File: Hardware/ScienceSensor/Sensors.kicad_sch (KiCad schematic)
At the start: 41 parts, among them J1 USB_A, Q2 BSS138, Q4 BSS138, U4 FT230XS

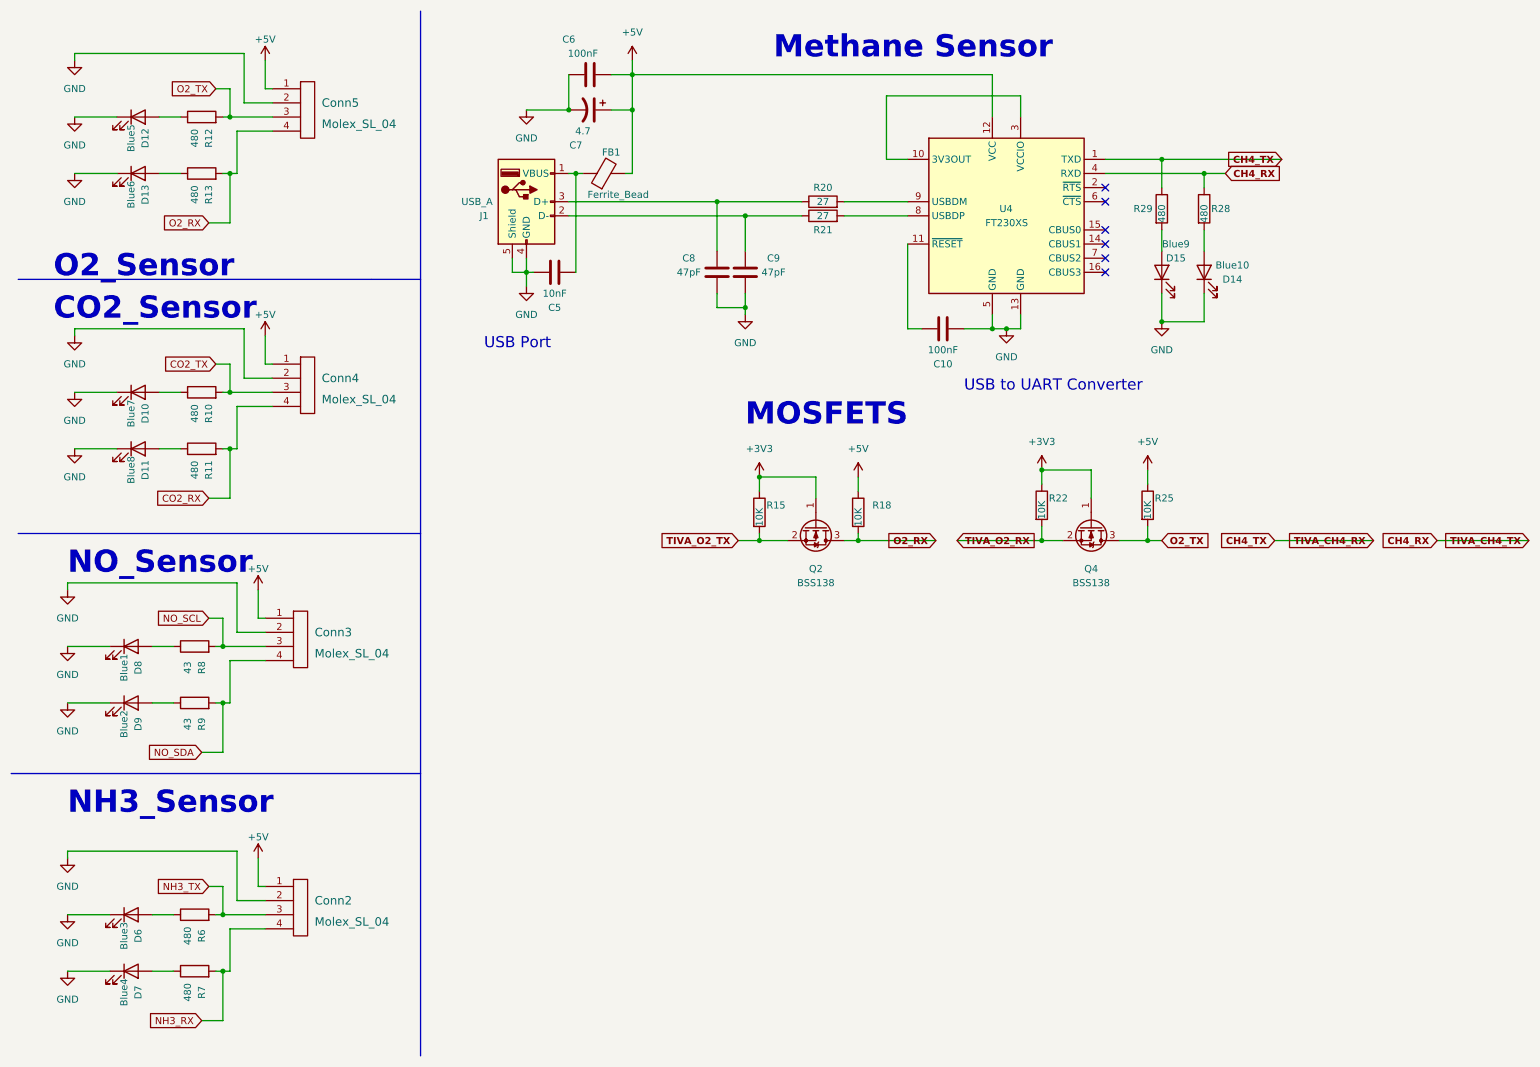
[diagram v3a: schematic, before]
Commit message: Fixed diode ref / values
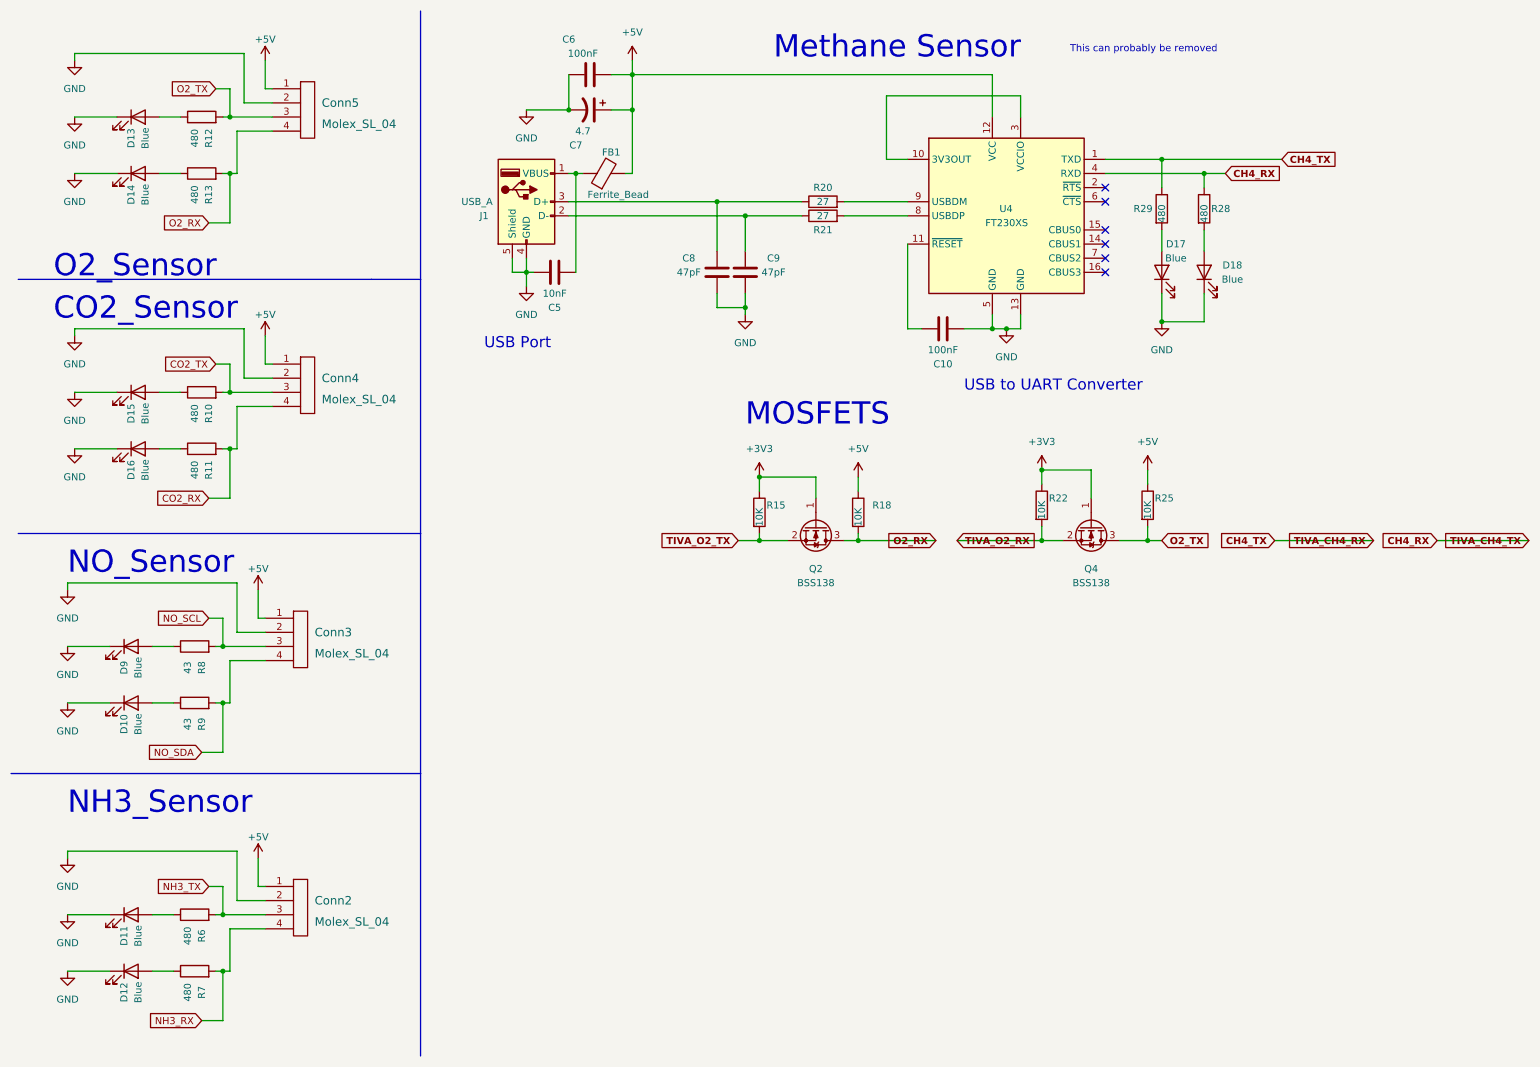
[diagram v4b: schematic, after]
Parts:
- D10: renamed from Blue2; value D9 -> Blue
- D11: renamed from Blue3; value D6 -> Blue
- D12: renamed from Blue4; value D7 -> Blue
- D13: renamed from Blue5; value D12 -> Blue
- D14: renamed from Blue6; value D13 -> Blue
- D15: renamed from Blue7; value D10 -> Blue
- D16: renamed from Blue8; value D11 -> Blue
- D17: renamed from Blue9; value D15 -> Blue
- D18: renamed from Blue10; value D14 -> Blue
- D9: renamed from Blue1; value D8 -> Blue
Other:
- note added: "This can probably be removed"
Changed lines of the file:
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@@
     (stroke (width 0) (type default) (color 0 0 0 0))
+  )
+  (text "This can probably be removed" (at 200.66 19.05 0)
+    (effects (font (size 1.27 1.27)) (justify left bottom))
   )
   (text "USB to UART Converter" (at 181.61 80.01 0)
@@
   )
   (text "Methane Sensor" (at 147.32 20.32 0)
-    (effects (font (size 4 4) bold) (justify left bottom))
+    (effects (font (size 4 4)) (justify left bottom))
   )
   (text "USB Port" (at 95.25 72.39 0)
@@
   )
   (text "MOSFETS" (at 142.24 86.36 0)
-    (effects (font (size 4 4) (thickness 0.6) bold) (justify left bottom))
+    (effects (font (size 4 4)) (justify left bottom))
   )
   (text "O2_Sensor" (at 17.78 59.69 0)
-    (effects (font (size 4 4) (thickness 1) bold) (justify left bottom))
+    (effects (font (size 4 4)) (justify left bottom))
   )
   (text "NO_Sensor" (at 20.32 113.03 0)
-    (effects (font (size 4 4) bold) (justify left bottom))
+    (effects (font (size 4 4)) (justify left bottom))
   )
   (text "NH3_Sensor" (at 20.32 156.21 0)
-    (effects (font (size 4 4) bold) (justify left bottom))
+    (effects (font (size 4 4)) (justify left bottom))
   )
   (text "CO2_Sensor" (at 17.78 67.31 0)
-    (effects (font (size 4 4) (thickness 1) bold) (justify left bottom))
+    (effects (font (size 4 4)) (justify left bottom))
   )
   (global_label "O2_RX" (shape input) (at 45.72 49.53 180) (fields_autoplaced)
@@
     )
   )
-  (global_label "CH4_TX" (shape input) (at 238.76 38.1 180) (fields_autoplaced)
-    (effects (font (size 1.27 1.27) bold) (justify right))
-    (property "Intersheet References" "${INTERSHEET_REFS}" (id 0) (at 229.2906 38.227 0)
-      (effects (font (size 1.27 1.27) bold) (justify right) hide)
+  (global_label "CH4_TX" (shape input) (at 238.76 38.1 0) (fields_autoplaced)
+    (effects (font (size 1.27 1.27) bold) (justify left))
+    (property "Intersheet References" "${INTERSHEET_REFS}" (id 0) (at 248.2294 37.973 0)
+      (effects (font (size 1.27 1.27) bold) (justify left) hide)
     )
   )
@@
   (symbol (lib_id "Device:LED") (at 31.75 135.89 0) (unit 1)
     (in_bom yes) (on_board yes)
-    (property "Reference" "Blue2" (id 0) (at 30.48 139.7 90))
-    (property "Value" "D9" (id 1) (at 33.02 139.7 90))
+    (property "Reference" "D10" (id 0) (at 30.48 139.7 90))
+    (property "Value" "Blue" (id 1) (at 33.02 139.7 90))
     (property "Footprint" "" (id 2) (at 31.75 135.89 0)
       (effects (font (size 1.27 1.27)) hide)
@@
   (symbol (lib_id "Device:LED") (at 224.79 58.42 90) (unit 1)
     (in_bom yes) (on_board yes)
-    (property "Reference" "Blue10" (id 0) (at 229.87 57.15 90))
-    (property "Value" "D14" (id 1) (at 229.87 59.69 90))
+    (property "Reference" "D18" (id 0) (at 229.87 57.15 90))
+    (property "Value" "Blue" (id 1) (at 229.87 59.69 90))
     (property "Footprint" "" (id 2) (at 224.79 58.42 0)
       (effects (font (size 1.27 1.27)) hide)
@@
   (symbol (lib_id "Device:LED") (at 33.02 90.17 0) (unit 1)
     (in_bom yes) (on_board yes)
-    (property "Reference" "Blue8" (id 0) (at 31.75 93.98 90))
-    (property "Value" "D11" (id 1) (at 34.29 93.98 90))
+    (property "Reference" "D16" (id 0) (at 31.75 93.98 90))
+    (property "Value" "Blue" (id 1) (at 34.29 93.98 90))
     (property "Footprint" "" (id 2) (at 33.02 90.17 0)
       (effects (font (size 1.27 1.27)) hide)
@@
   (symbol (lib_id "Device:LED") (at 31.75 173.99 0) (unit 1)
     (in_bom yes) (on_board yes)
-    (property "Reference" "Blue3" (id 0) (at 30.48 177.8 90))
-    (property "Value" "D6" (id 1) (at 33.02 177.8 90))
+    (property "Reference" "D11" (id 0) (at 30.48 177.8 90))
+    (property "Value" "Blue" (id 1) (at 33.02 177.8 90))
     (property "Footprint" "" (id 2) (at 31.75 173.99 0)
       (effects (font (size 1.27 1.27)) hide)
@@
   (symbol (lib_id "Device:LED") (at 31.75 125.73 0) (unit 1)
     (in_bom yes) (on_board yes)
-    (property "Reference" "Blue1" (id 0) (at 30.48 129.54 90))
-    (property "Value" "D8" (id 1) (at 33.02 129.54 90))
+    (property "Reference" "D9" (id 0) (at 30.48 129.54 90))
+    (property "Value" "Blue" (id 1) (at 33.02 129.54 90))
     (property "Footprint" "" (id 2) (at 31.75 125.73 0)
       (effects (font (size 1.27 1.27)) hide)
@@
   (symbol (lib_id "Device:LED") (at 33.02 30.48 0) (unit 1)
     (in_bom yes) (on_board yes)
-    (property "Reference" "Blue5" (id 0) (at 31.75 34.29 90))
-    (property "Value" "D12" (id 1) (at 34.29 34.29 90))
+    (property "Reference" "D13" (id 0) (at 31.75 34.29 90))
+    (property "Value" "Blue" (id 1) (at 34.29 34.29 90))
     (property "Footprint" "" (id 2) (at 33.02 30.48 0)
       (effects (font (size 1.27 1.27)) hide)
@@
   (symbol (lib_id "Device:LED") (at 33.02 40.64 0) (unit 1)
     (in_bom yes) (on_board yes)
-    (property "Reference" "Blue6" (id 0) (at 31.75 44.45 90))
-    (property "Value" "D13" (id 1) (at 34.29 44.45 90))
+    (property "Reference" "D14" (id 0) (at 31.75 44.45 90))
+    (property "Value" "Blue" (id 1) (at 34.29 44.45 90))
     (property "Footprint" "" (id 2) (at 33.02 40.64 0)
       (effects (font (size 1.27 1.27)) hide)
@@
   (symbol (lib_id "Device:LED") (at 217.17 58.42 90) (unit 1)
     (in_bom yes) (on_board yes)
-    (property "Reference" "Blue9" (id 0) (at 219.71 53.34 90))
-    (property "Value" "D15" (id 1) (at 219.71 55.88 90))
+    (property "Reference" "D17" (id 0) (at 219.71 53.34 90))
+    (property "Value" "Blue" (id 1) (at 219.71 55.88 90))
     (property "Footprint" "" (id 2) (at 217.17 58.42 0)
       (effects (font (size 1.27 1.27)) hide)
@@
   (symbol (lib_id "Device:LED") (at 33.02 80.01 0) (unit 1)
     (in_bom yes) (on_board yes)
-    (property "Reference" "Blue7" (id 0) (at 31.75 83.82 90))
-    (property "Value" "D10" (id 1) (at 34.29 83.82 90))
+    (property "Reference" "D15" (id 0) (at 31.75 83.82 90))
+    (property "Value" "Blue" (id 1) (at 34.29 83.82 90))
     (property "Footprint" "" (id 2) (at 33.02 80.01 0)
       (effects (font (size 1.27 1.27)) hide)
@@
   (symbol (lib_id "Device:LED") (at 31.75 184.15 0) (unit 1)
     (in_bom yes) (on_board yes)
-    (property "Reference" "Blue4" (id 0) (at 30.48 187.96 90))
-    (property "Value" "D7" (id 1) (at 33.02 187.96 90))
+    (property "Reference" "D12" (id 0) (at 30.48 187.96 90))
+    (property "Value" "Blue" (id 1) (at 33.02 187.96 90))
     (property "Footprint" "" (id 2) (at 31.75 184.15 0)
       (effects (font (size 1.27 1.27)) hide)

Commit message: Mosfets added, NO sensor updated, NH3 removed NO2 added
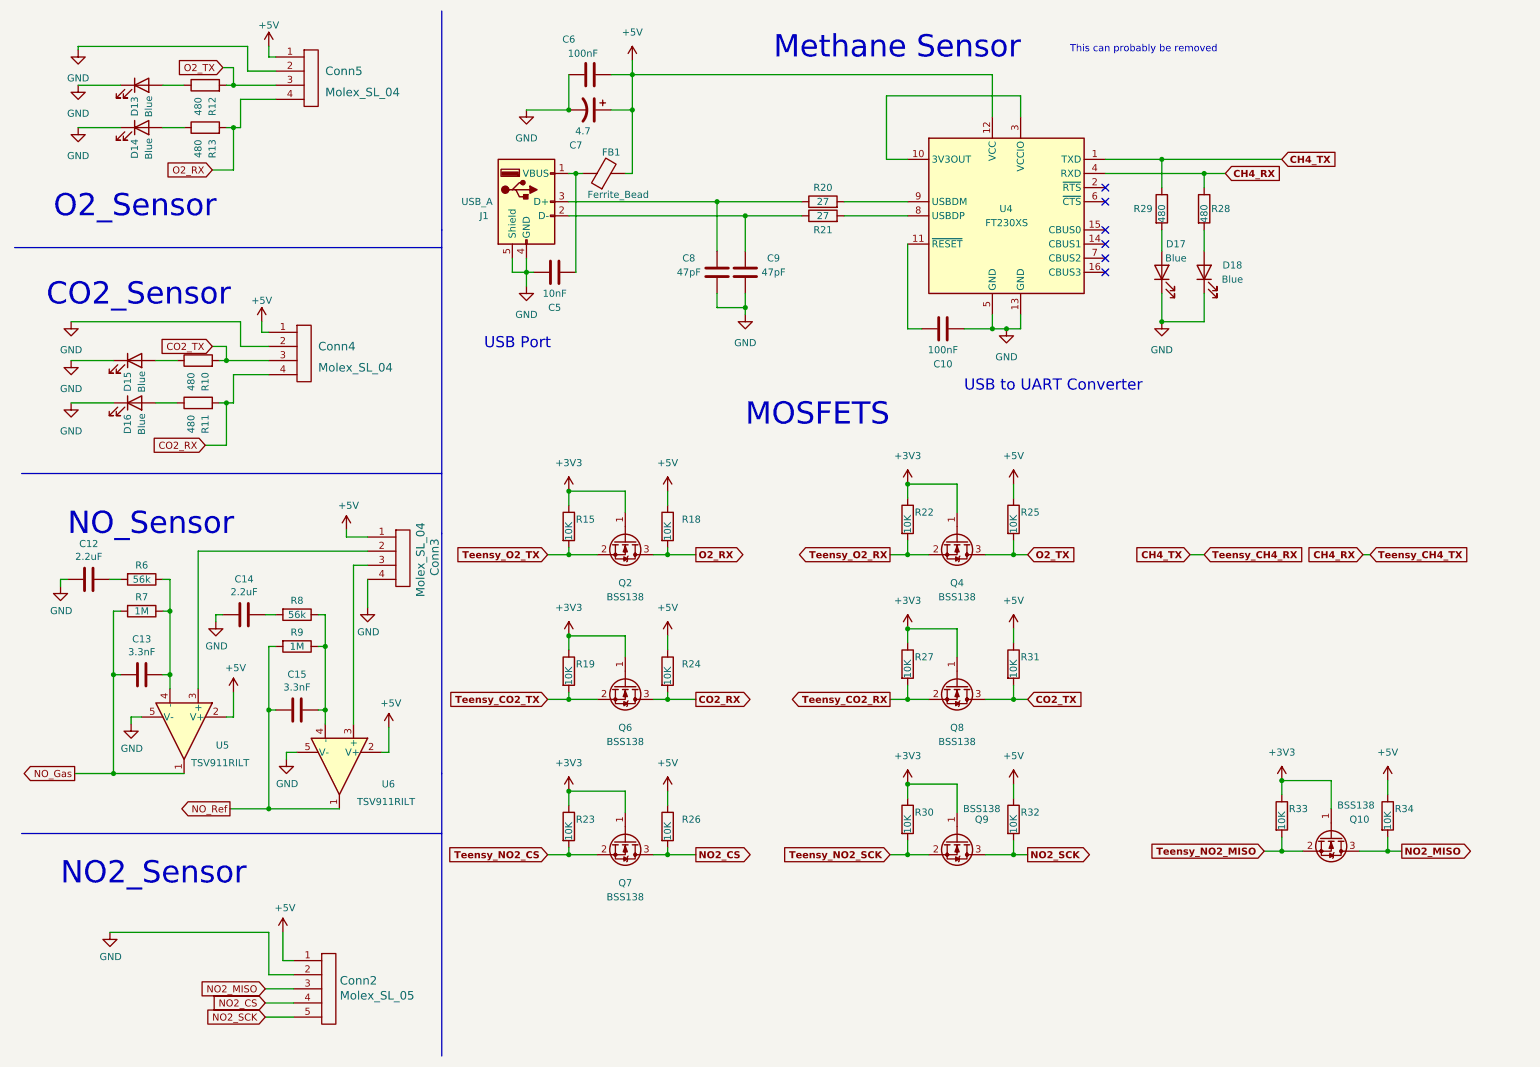
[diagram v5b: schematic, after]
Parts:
- removed Conn2: Molex_SL_04, symbol MRDT_Connectors:Molex_SL_04
- removed D10, D11, D12, D9: Blue, symbol Device:LED
- added C12, C14: 2.2uF, Capacitor_SMD:C_0603_1608Metric_Pad1.08x0.95mm_HandSolder, symbol Device:C
- added C13, C15: 3.3nF, Capacitor_SMD:C_0603_1608Metric_Pad1.08x0.95mm_HandSolder, symbol Device:C
- added Conn2: Molex_SL_05, MRDT_Connectors:MOLEX_SL_05_Horizontal, symbol MRDT_Connectors:Molex_SL_05
- added Q10, Q6, Q7, Q8, Q9: BSS138, symbol Device:Q_NMOS_GSD
- added R19, R23, R24, R26, R27, R30, R31, R32, R33, R34: 10K, symbol Device:R
- added U5, U6: TSV911RILT, Package_TO_SOT_SMD:SOT-23-5, symbol Amplifier_Operational:TSV911RILT
- Conn3: footprint (none) -> MRDT_Connectors:MOLEX_SL_04_Horizontal
- R6: value 480 -> 56k; footprint (none) -> Resistor_SMD:R_0603_1608Metric_Pad0.98x0.95mm_HandSolder
- R7: value 480 -> 1M; footprint (none) -> Resistor_SMD:R_0603_1608Metric_Pad0.98x0.95mm_HandSolder
- R8: value 43 -> 56k; footprint (none) -> Resistor_SMD:R_0603_1608Metric_Pad0.98x0.95mm_HandSolder
- R9: value 43 -> 1M; footprint (none) -> Resistor_SMD:R_0603_1608Metric_Pad0.98x0.95mm_HandSolder
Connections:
- net +3V3: now also Q10.1 (G), Q6.1 (G), Q7.1 (G), Q8.1 (G), Q9.1 (G), R19.1, R23.1, R27.1, R30.1, R33.1
- net +5V: now also Conn2.1, R24.1, R26.1, R31.1, R32.1, R34.1, U5.2 (V+), U6.2 (V+)
- net CO2_RX: now also Q6.3 (D), R24.2
- net CO2_TX: now also Q8.3 (D), R31.2
- net GND: now also Conn3.4, C12.2, C14.2, Conn2.2, U5.5 (V-), U6.5 (V-); no longer Conn3.2
- net at R7.1: now also R6.1, C13.1, U5.4 (-)
- net at R9.1: now also R8.1, C15.1, U6.4 (-)
- net NH3_RX renamed NO_Gas
- net NO_Gas: now also C13.2, U5.1
- net NH3_TX: no longer names the net of R6.2
- net NH3_TX: now also C12.1
- net NO_SCL: no longer names the net of R8.2
- net NO_SCL: now also C14.1; no longer Conn3.3
- net NO_SDA renamed NO_Ref
- net NO_Ref: now also C15.2, U6.1; no longer Conn3.4
- net TIVA_O2_RX renamed Teensy_O2_RX
- net TIVA_O2_TX renamed Teensy_O2_TX
- new net: Conn3.2, U5.3 (+)
- new net: Conn3.3, U6.3 (+)
- new net NO2_CS: Conn2.4, Q7.3 (D), R26.2
- new net NO2_MISO: Conn2.3, Q10.3 (D), R34.2
- new net NO2_SCK: Conn2.5, Q9.3 (D), R32.2
- new net Teensy_CO2_RX: Q8.2 (S), R27.2
- new net Teensy_CO2_TX: Q6.2 (S), R19.2
- new net Teensy_NO2_CS: Q7.2 (S), R23.2
- new net Teensy_NO2_MISO: Q10.2 (S), R33.2
- new net Teensy_NO2_SCK: Q9.2 (S), R30.2
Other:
- note added: "NO2_Sensor"
- note removed: "NH3_Sensor"
- moved on the sheet: Conn4, Conn5, D13, D14, D15, D16, Q2, Q4, R10, R11, R12, R13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
